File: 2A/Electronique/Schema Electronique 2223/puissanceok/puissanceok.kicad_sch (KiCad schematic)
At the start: 33 parts, among them J10 Conn_01x05, J11 Conn_01x02, J12 Conn_01x02, J13 Conn_01x02, J14 Conn_01x02, J15 Conn_01x02, J5 Conn_01x08, J6 Conn_01x08, J7 Conn_01x08, J9 Conn_01x05

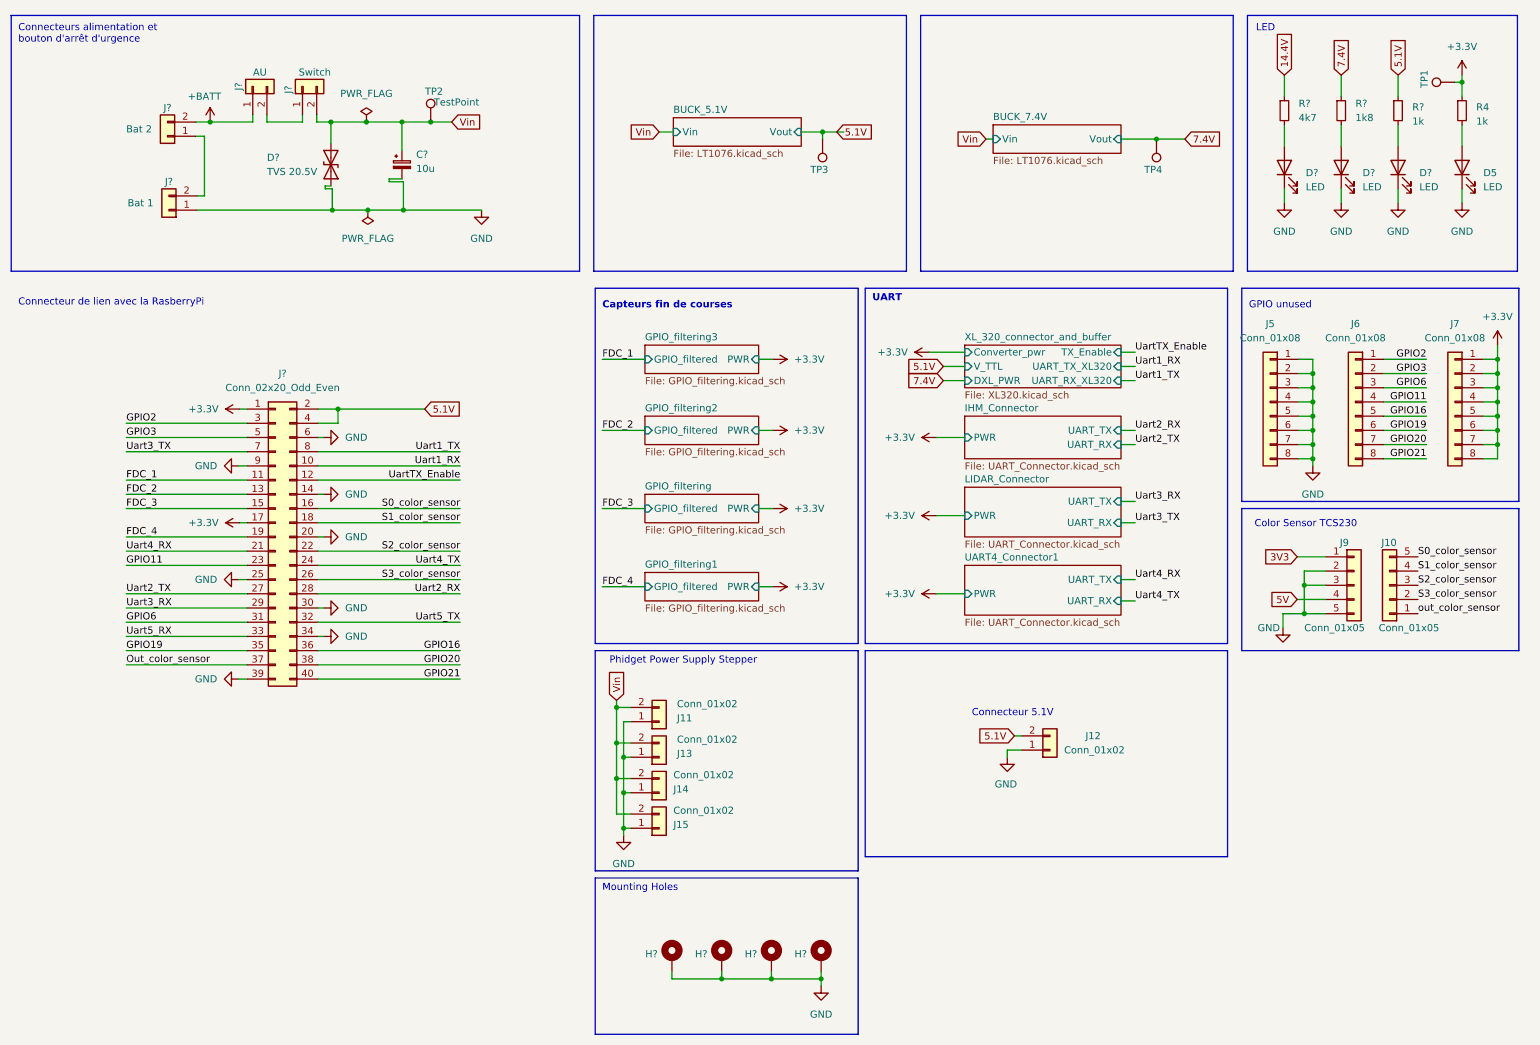
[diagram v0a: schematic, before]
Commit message: add schematic update and footprint
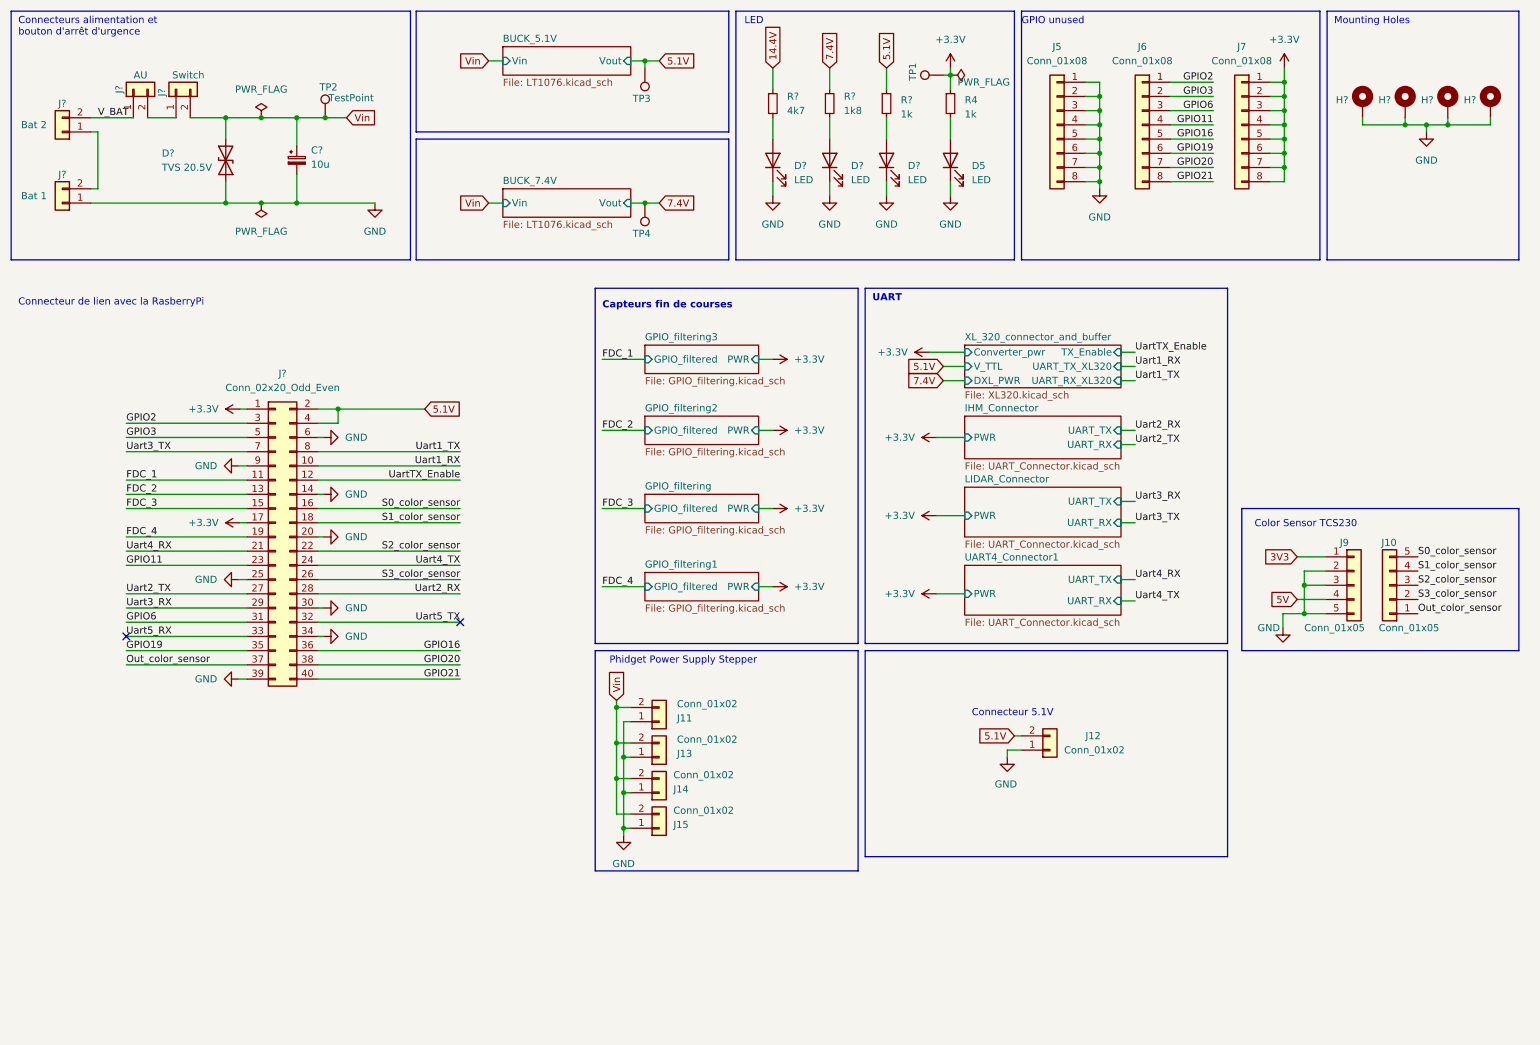
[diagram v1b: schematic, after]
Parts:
- C?: footprint (none) -> Capacitor_SMD:CP_Elec_4x5.4; MPN 865080642006 -> 865060440001; Vmax (none) -> 25V
- D?: footprint (none) -> Diode_SMD:D_SMB
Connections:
- net out_color_sensor is gone; now on net Out_color_sensor: J10.1 (Pin_1)
- net +BATT renamed V_BAT
- no-connect marks 0 -> 2
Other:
- moved on the sheet: C?, D5, D?, H?, J5, J6, J7, J?, R4, R?, TP1, TP2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

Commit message: finalize schematic + footprints
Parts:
- H? (x4): footprint MountingHole:MountingHole_3.2mm_M3_Pad_Via -> MountingHole:MountingHole_2.7mm_M2.5_Pad_Via
- J11: value Conn_01x02 -> Conn_Phidget_PS_Stepper_1
- J13: value Conn_01x02 -> Conn_Phidget_PS_Stepper_2
- J14: value Conn_01x02 -> Conn_Phidget_PS_Stepper_3
- J15: value Conn_01x02 -> Conn_Phidget_PS_Stepper_4
- J5: value Conn_01x08 -> Conn_GND
- J6: value Conn_01x08 -> Conn_GPIO_unused
- J7: value Conn_01x08 -> Conn_3.3V
- J? (x4): footprint (none) -> custom:691322110002; MPN (none) -> 691322110002
- J?: value Conn_02x20_Odd_Even -> Conn_RPI
- R4, R? (x3): footprint Resistor_SMD:R_0603_1608Metric_Pad0.98x0.95mm_HandSolder -> Resistor_SMD:R_0402_1005Metric
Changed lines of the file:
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@@
       (effects (font (size 1.27 1.27)) (justify left))
     )
-    (property "Footprint" "Resistor_SMD:R_0603_1608Metric_Pad0.98x0.95mm_HandSolder" (at 181.61 30.48 0)
+    (property "Footprint" "Resistor_SMD:R_0402_1005Metric" (at 181.61 30.48 0)
       (effects (font (size 1.27 1.27)) hide)
     )
@@
       (effects (font (size 1.27 1.27)) (justify right) hide)
     )
-    (property "Footprint" "MountingHole:MountingHole_3.2mm_M3_Pad_Via" (at 262.89 30.48 0)
+    (property "Footprint" "MountingHole:MountingHole_2.7mm_M2.5_Pad_Via" (at 262.89 30.48 0)
       (effects (font (size 1.27 1.27)) hide)
     )
@@
       (effects (font (size 1.27 1.27)))
     )
-    (property "Footprint" "" (at 22.86 48.26 0)
-      (effects (font (size 1.27 1.27)) hide)
-    )
-    (property "Datasheet" "~" (at 22.86 48.26 0)
+    (property "Footprint" "custom:691322110002" (at 22.86 48.26 0)
+      (effects (font (size 1.27 1.27)) hide)
+    )
+    (property "Datasheet" "https://www.we-online.com/components/products/datasheet/691322110002.pdf" (at 22.86 48.26 0)
+      (effects (font (size 1.27 1.27)) hide)
+    )
+    (property "MPN" "691322110002" (at 22.86 48.26 0)
       (effects (font (size 1.27 1.27)) hide)
     )
@@
       (effects (font (size 1.27 1.27)) (justify left))
     )
-    (property "Value" "Conn_01x02" (at 132.715 144.145 0)
+    (property "Value" "Conn_Phidget_PS_Stepper_2" (at 132.715 144.145 0)
       (effects (font (size 1.27 1.27)) (justify left))
     )
@@
       (effects (font (size 1.27 1.27)) (justify left))
     )
-    (property "Value" "Conn_01x02" (at 132.715 137.795 0)
+    (property "Value" "Conn_Phidget_PS_Stepper_1" (at 132.715 137.795 0)
       (effects (font (size 1.27 1.27)) (justify left))
     )
@@
       (effects (font (size 1.27 1.27)) (justify left))
     )
-    (property "Value" "Conn_01x02" (at 132.08 156.845 0)
+    (property "Value" "Conn_Phidget_PS_Stepper_4" (at 132.08 156.845 0)
       (effects (font (size 1.27 1.27)) (justify left))
     )
@@
   )
   (symbol (lib_id "Connector_Generic:Conn_01x08") (at 215.9 34.29 0) (mirror y) (unit 1)
-    (in_bom yes) (on_board yes) (dnp no) (fields_autoplaced)
+    (in_bom yes) (on_board yes) (dnp no)
     (property "Reference" "J6" (at 215.9 20.32 0)
       (effects (font (size 1.27 1.27)))
     )
-    (property "Value" "Conn_01x08" (at 215.9 22.86 0)
+    (property "Value" "Conn_GPIO_unused" (at 218.44 22.86 0)
       (effects (font (size 1.27 1.27)))
     )
@@
       (effects (font (size 1.27 1.27)))
     )
-    (property "Value" "Conn_01x08" (at 200.66 22.86 0)
+    (property "Value" "Conn_GND" (at 200.66 22.86 0)
       (effects (font (size 1.27 1.27)))
     )
@@
       (effects (font (size 1.27 1.27)))
     )
-    (property "Footprint" "" (at 35.56 27.94 0)
-      (effects (font (size 1.27 1.27)) hide)
-    )
-    (property "Datasheet" "~" (at 35.56 27.94 0)
+    (property "Footprint" "custom:691322110002" (at 35.56 27.94 0)
+      (effects (font (size 1.27 1.27)) hide)
+    )
+    (property "Datasheet" "https://www.we-online.com/components/products/datasheet/691322110002.pdf" (at 35.56 27.94 0)
+      (effects (font (size 1.27 1.27)) hide)
+    )
+    (property "MPN" "691322110002" (at 35.56 27.94 0)
       (effects (font (size 1.27 1.27)) hide)
     )
@@
       (effects (font (size 1.27 1.27)) (justify left))
     )
-    (property "Value" "Conn_01x02" (at 132.08 150.495 0)
+    (property "Value" "Conn_Phidget_PS_Stepper_3" (at 132.08 150.495 0)
       (effects (font (size 1.27 1.27)) (justify left))
     )
@@
       (effects (font (size 1.27 1.27)))
     )
-    (property "Value" "Conn_02x20_Odd_Even" (at 62.23 81.28 0)
+    (property "Value" "Conn_RPI" (at 62.23 81.28 0)
       (effects (font (size 1.27 1.27)))
     )
@@
       (effects (font (size 1.27 1.27)))
     )
-    (property "Value" "Conn_01x08" (at 233.68 22.86 0)
+    (property "Value" "Conn_3.3V" (at 233.68 22.86 0)
       (effects (font (size 1.27 1.27)))
     )
@@
       (effects (font (size 1.27 1.27)) (justify left))
     )
-    (property "Footprint" "Resistor_SMD:R_0603_1608Metric_Pad0.98x0.95mm_HandSolder" (at 149.86 30.48 0)
+    (property "Footprint" "Resistor_SMD:R_0402_1005Metric" (at 149.86 30.48 0)
       (effects (font (size 1.27 1.27)) hide)
     )
@@
       (effects (font (size 1.27 1.27)) (justify right) hide)
     )
-    (property "Footprint" "MountingHole:MountingHole_3.2mm_M3_Pad_Via" (at 255.27 30.48 0)
+    (property "Footprint" "MountingHole:MountingHole_2.7mm_M2.5_Pad_Via" (at 255.27 30.48 0)
       (effects (font (size 1.27 1.27)) hide)
     )
@@
       (effects (font (size 1.27 1.27)) (justify left))
     )
-    (property "Footprint" "" (at 43.18 27.94 0)
-      (effects (font (size 1.27 1.27)) hide)
-    )
-    (property "Datasheet" "~" (at 43.18 27.94 0)
+    (property "Footprint" "custom:691322110002" (at 43.18 27.94 0)
+      (effects (font (size 1.27 1.27)) hide)
+    )
+    (property "Datasheet" "https://www.we-online.com/components/products/datasheet/691322110002.pdf" (at 43.18 27.94 0)
+      (effects (font (size 1.27 1.27)) hide)
+    )
+    (property "MPN" "691322110002" (at 43.18 27.94 0)
       (effects (font (size 1.27 1.27)) hide)
     )
@@
       (effects (font (size 1.27 1.27)) (justify left))
     )
-    (property "Footprint" "Resistor_SMD:R_0603_1608Metric_Pad0.98x0.95mm_HandSolder" (at 160.02 30.48 0)
+    (property "Footprint" "Resistor_SMD:R_0402_1005Metric" (at 160.02 30.48 0)
       (effects (font (size 1.27 1.27)) hide)
     )
@@
       (effects (font (size 1.27 1.27)) (justify right) hide)
     )
-    (property "Footprint" "MountingHole:MountingHole_3.2mm_M3_Pad_Via" (at 270.51 30.48 0)
+    (property "Footprint" "MountingHole:MountingHole_2.7mm_M2.5_Pad_Via" (at 270.51 30.48 0)
       (effects (font (size 1.27 1.27)) hide)
     )
@@
       (effects (font (size 1.27 1.27)) (justify right) hide)
     )
-    (property "Footprint" "MountingHole:MountingHole_3.2mm_M3_Pad_Via" (at 278.13 30.48 0)
+    (property "Footprint" "MountingHole:MountingHole_2.7mm_M2.5_Pad_Via" (at 278.13 30.48 0)
       (effects (font (size 1.27 1.27)) hide)
     )
@@
       (effects (font (size 1.27 1.27)) (justify left))
     )
-    (property "Footprint" "Resistor_SMD:R_0603_1608Metric_Pad0.98x0.95mm_HandSolder" (at 170.18 30.48 0)
+    (property "Footprint" "Resistor_SMD:R_0402_1005Metric" (at 170.18 30.48 0)
       (effects (font (size 1.27 1.27)) hide)
     )
@@
       (effects (font (size 1.27 1.27)))
     )
-    (property "Footprint" "" (at 22.86 35.56 0)
-      (effects (font (size 1.27 1.27)) hide)
-    )
-    (property "Datasheet" "~" (at 22.86 35.56 0)
-      (effects (font (size 1.27 1.27)) hide)
-    )
+    (property "Footprint" "custom:691322110002" (at 22.86 35.56 0)
+      (effects (font (size 1.27 1.27)) hide)
+    )
+    (property "Datasheet" "https://www.we-online.com/components/products/datasheet/691322110002.pdf" (at 22.86 35.56 0)
+      (effects (font (size 1.27 1.27)) hide)
+    )
+    (property "MPN" "691322110002" (at 22.86 35.56 0)
+      (effects (font (size 1.27 1.27)) hide)
+    )

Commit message: update pcb and schematic
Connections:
- net 14.4V is gone; now on net Vin: R?.1
- net 3V3 is gone; now on net +3.3V: J9.1 (Pin_1)
- net 5V is gone; now on net 5.1V: J9.4 (Pin_4)
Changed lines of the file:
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@@
-    (stroke (width 0) (type default))
-  )
-  (wire (pts (xy 243.586 111.506) (xy 248.666 111.506))
     (stroke (width 0) (type default))
   )
@@
     (stroke (width 0) (type default))
   )
+  (wire (pts (xy 242.9656 111.6259) (xy 242.9656 111.506))
+    (stroke (width 0) (type default))
+  )
   (wire (pts (xy 170.18 46.99) (xy 170.18 44.45))
     (stroke (width 0) (type default))
@@
   )
   (wire (pts (xy 34.29 107.95) (xy 55.88 107.95))
+    (stroke (width 0) (type default))
+  )
+  (wire (pts (xy 242.9656 111.506) (xy 248.666 111.506))
     (stroke (width 0) (type default))
   )
@@
     )
   )
-  (global_label "14.4V" (shape input) (at 149.86 24.13 90) (fields_autoplaced)
+  (global_label "Vin" (shape input) (at 149.86 24.13 90) (fields_autoplaced)
     (effects (font (size 1.27 1.27)) (justify left))
-    (property "Intersheetrefs" "${INTERSHEET_REFS}" (at 149.86 15.8229 90)
+    (property "Intersheetrefs" "${INTERSHEET_REFS}" (at 149.86 18.3024 90)
       (effects (font (size 1.27 1.27)) (justify left) hide)
     )
@@
     )
   )
-  (global_label "5V" (shape input) (at 243.586 119.126 180) (fields_autoplaced)
+  (global_label "5.1V" (shape input) (at 243.586 119.126 180) (fields_autoplaced)
     (effects (font (size 1.27 1.27)) (justify right))
-    (property "Intersheetrefs" "${INTERSHEET_REFS}" (at 238.3027 119.126 0)
+    (property "Intersheetrefs" "${INTERSHEET_REFS}" (at 236.4884 119.126 0)
       (effects (font (size 1.27 1.27)) (justify right) hide)
     )
@@
     )
   )
-  (global_label "3V3" (shape input) (at 243.586 111.506 180) (fields_autoplaced)
-    (effects (font (size 1.27 1.27)) (justify right))
-    (property "Intersheetrefs" "${INTERSHEET_REFS}" (at 237.0932 111.506 0)
-      (effects (font (size 1.27 1.27)) (justify right) hide)
-    )
-  )
   (symbol (lib_id "Device:LED") (at 149.86 40.64 90) (unit 1)
     (in_bom yes) (on_board yes) (dnp no) (fields_autoplaced)
@@
         )
       )
+    )
+  )
+  (symbol (lib_id "power:+3.3V") (at 242.9656 111.6259 90) (unit 1)
+    (in_bom yes) (on_board yes) (dnp no) (fields_autoplaced)
+    (property "Reference" "#PWR02" (at 246.7756 111.6259 0)
+      (effects (font (size 1.27 1.27)) hide)
+    )
+    (property "Value" "+3.3V" (at 239.1556 111.6259 90)
+      (effects (font (size 1.27 1.27)) (justify left))
+    )
+    (property "Footprint" "" (at 242.9656 111.6259 0)
+      (effects (font (size 1.27 1.27)) hide)
+    )
+    (property "Datasheet" "" (at 242.9656 111.6259 0)
+      (effects (font (size 1.27 1.27)) hide)
+    )
+    (pin "1")
+    (instances
+      (project "puissanceok"
+        (path "/50648b18-b1a7-4d76-a5dd-1fad5f3e825e"
+          (reference "#PWR02") (unit 1)
+        )
+      )
